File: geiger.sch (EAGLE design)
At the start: 4 parts, among them IC1 74LS14D, IC4 ICL7621SA

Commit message: Picking parts
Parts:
- removed D1: 1N821, diode:1N821
- removed IC4: ICL7621SA, maxim:ICL7621SA
- added C1, C10, C11, C12, C13, C14, C15, C16, C2, C3, C4, C5, C6, C7, C8, C9: (no value), rcl:C-EUC0603
- added D10, D11, D12, D13, D14, D15, D16, D17, D2, D3, D4, D5, D6, D7, D8, D9: 1N4148DO35-7, diode:1N4148DO35-7
- added IC2: LM4041A12DBZ, texas:LM4041A12DBZ
- added IC3: MAX4105EUK, maxim:MAX4105EUK
- added L1: (no value), rcl:L-US6000-XXX-RC
- added R1, R2, R3, R4, R5: (no value), resistor:R-EU_R0603
- added R6: (no value), rcl:R-TRIMM4G/J
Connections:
- new net F/B: IC3G$1.-IN, R4.1, R5.2
- new net N$10: C3.2, C5.1, D5.A
- new net N$11: R6.E
- new net N$12: C5.2, C7.1, D6.C, D7.A
- new net N$13: C6.2, C8.1, D7.C, D8.A
- new net N$14: C7.2, C9.1, D8.C, D9.A
- new net N$15: C10.1, C8.2, D10.A, D9.C
- new net N$16: C11.1, C9.2, D10.C, D11.A
- new net N$17: C11.2, C13.1, D12.C, D13.A
- new net N$18: C13.2, C15.1, D14.C, D15.A
- new net N$19: C15.2, D16.C, D17.A
- new net N$2: D2.A, R3.1
- new net N$20: C16.2, D17.C
- new net N$21: C14.2, C16.1, D15.C, D16.A
- new net N$22: C12.2, C14.1, D13.C, D14.A
- new net N$23: C10.2, C12.1, D11.C, D12.A
- new net N$24: C3.1, D3.A, L1.2
- new net N$7: C2.2, C4.1, D3.C, D4.A, R4.2
- new net N$8: C4.2, C6.1, D5.C, D6.A
- net GND: now also C1.2, C2.1, IC2.A, R6.S; no longer D1.A, IC4A.V-
- net N$1: now also IC2.C, IC3G$1.+IN, R1.1; no longer D1.C, IC4A.+IN
- net N$3: now also IC3G$1.OUT, R2.2; no longer IC4A.OUT
- net N$4: now also C1.1, R2.1, R3.2
- net N$5: now also D2.C
- net VCC: now also L1.1, R1.2; no longer IC4A.V+
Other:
- moved on the sheet: Q1

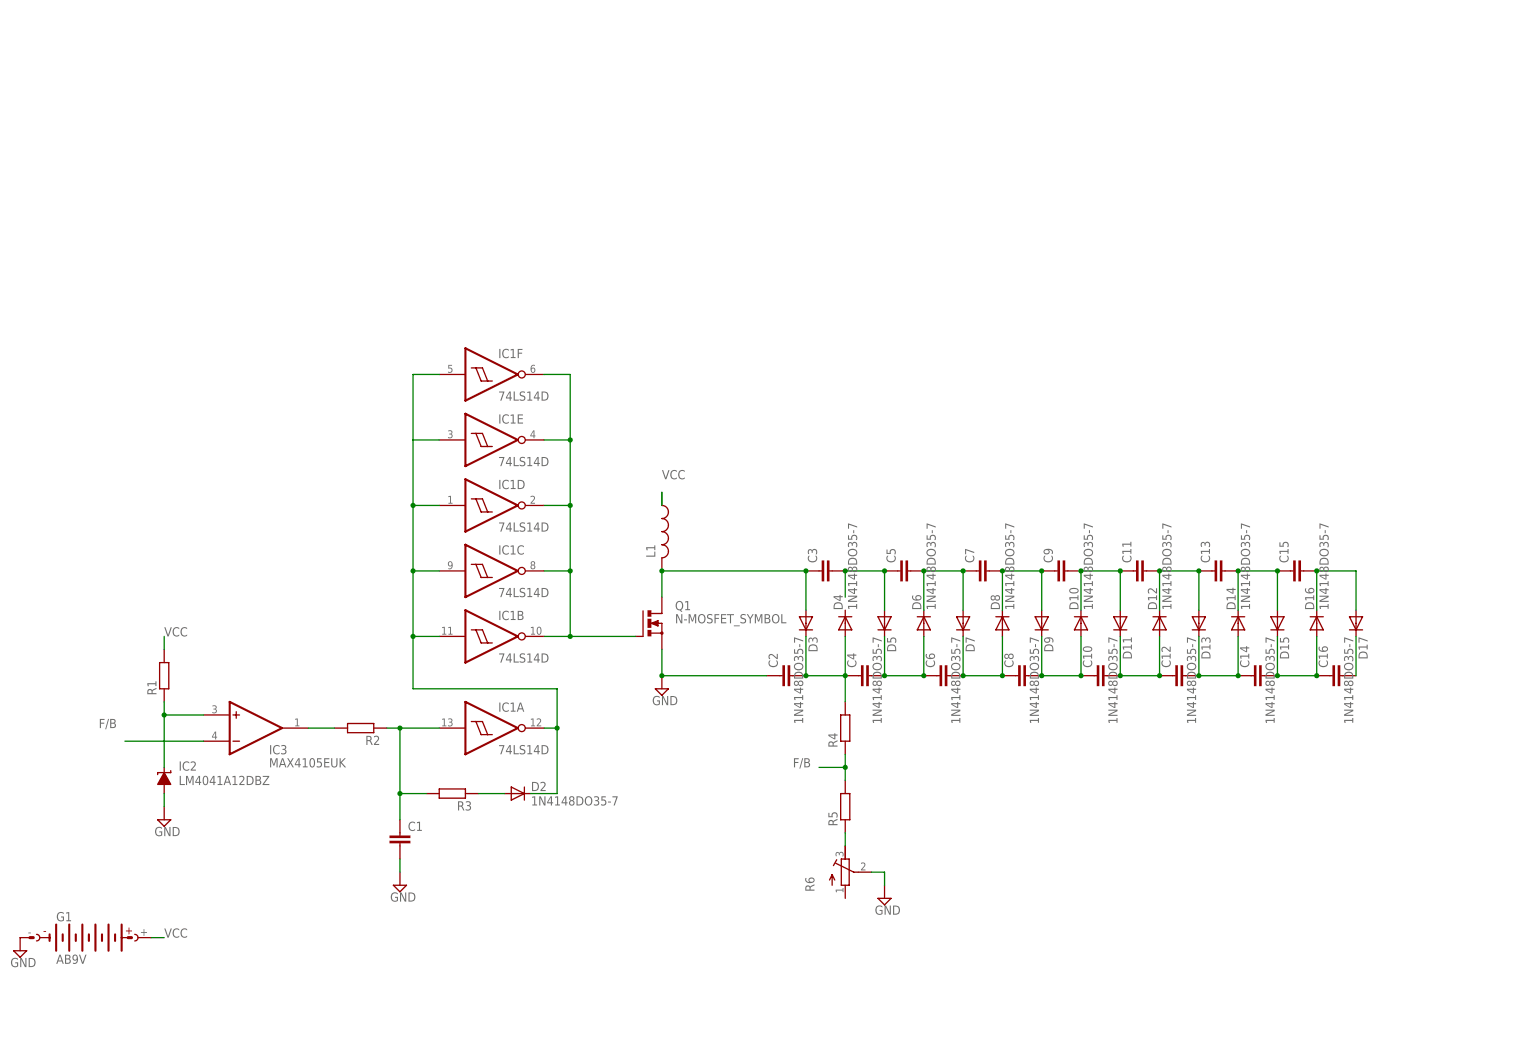
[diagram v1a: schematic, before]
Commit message: Completeing power supply on board
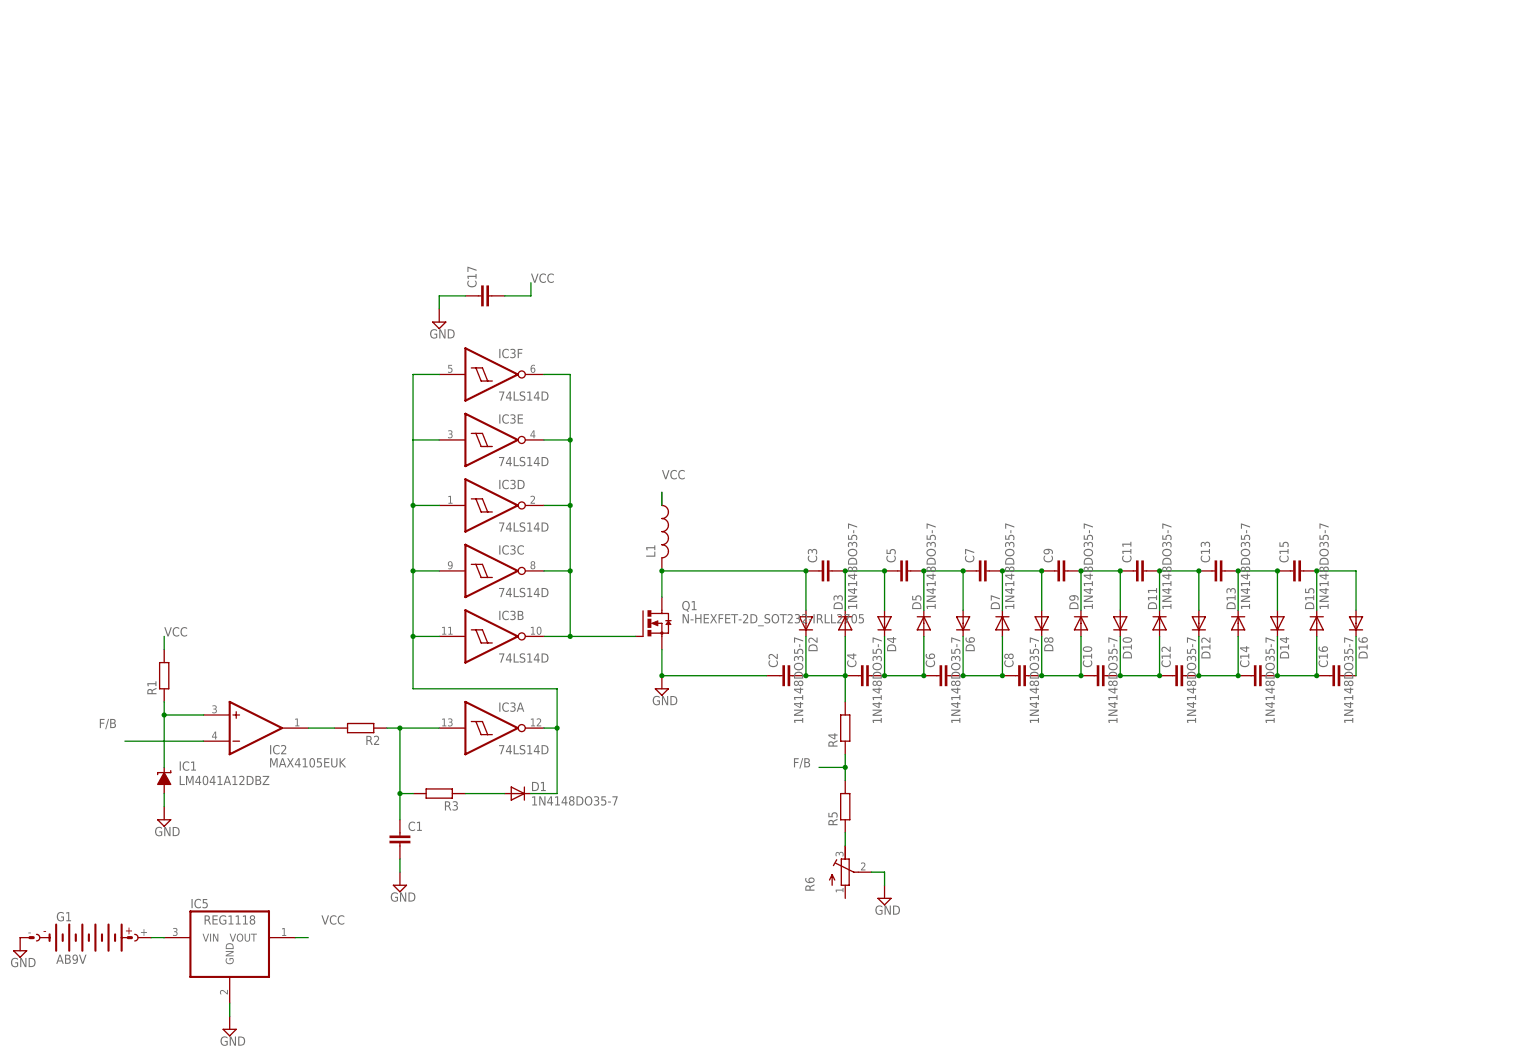
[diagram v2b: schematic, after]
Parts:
- removed D17: 1N4148DO35-7, diode:1N4148DO35-7
- added C17: (no value), rcl:C-EUC0603
- added D1: 1N4148DO35-7, diode:1N4148DO35-7
- added IC5: REG1118, burr-brown:REG1118
- added Q1: N-HEXFET-2D_SOT232-IRLL2705, transistor-power:N-HEXFET-2D_SOT232-IRLL2705
- IC1: value 74LS14D -> LM4041A12DBZ; device 74xx-us:74LS14D -> texas:LM4041A12DBZ
- IC2: value LM4041A12DBZ -> MAX4105EUK; device texas:LM4041A12DBZ -> maxim:MAX4105EUK
- IC3: value MAX4105EUK -> 74LS14D; device maxim:MAX4105EUK -> 74xx-us:74LS14D
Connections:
- new net N$9: G1.+, IC5.VIN
- net F/B: now also IC2G$1.-IN; no longer IC3G$1.-IN
- net GND: now also C17.1, IC1.A, IC5.GND, Q1.S; no longer IC2.A
- net N$1: now also IC1.C, IC2G$1.+IN; no longer IC2.C, IC3G$1.+IN
- net N$10: now also D3.C, D4.A; no longer D5.A
- net N$11: now also R5.1
- net N$12: now also D5.C, D6.A; no longer D6.C, D7.A
- net N$13: now also D6.C, D7.A; no longer D7.C, D8.A
- net N$14: now also D7.C, D8.A; no longer D8.C, D9.A
- net N$15: now also D8.C, D9.A; no longer D10.A, D9.C
- net N$16: now also D10.A, D9.C; no longer D10.C, D11.A
- net N$17: now also D11.C, D12.A; no longer D12.C, D13.A
- net N$18: now also D13.C, D14.A; no longer D14.C, D15.A
- net N$19: now also D15.C, D16.A; no longer D16.C, D17.A
- net N$2: now also D1.A; no longer D2.A
- net N$20: now also D16.C; no longer D17.C
- net N$21: now also D14.C, D15.A; no longer D15.C, D16.A
- net N$22: now also D12.C, D13.A; no longer D13.C, D14.A
- net N$23: now also D10.C, D11.A; no longer D11.C, D12.A
- net N$24: now also D2.A, Q1.D; no longer D3.A
- net N$3: now also IC2G$1.OUT; no longer IC3G$1.OUT
- net N$4: now also IC3A.I; no longer IC1A.I
- net N$5: now also D1.C, IC3A.O, IC3B.I, IC3C.I, IC3D.I, IC3E.I, IC3F.I; no longer D2.C, IC1A.O, IC1B.I, IC1C.I, IC1D.I, IC1E.I, IC1F.I
- net N$6: now also IC3B.O, IC3C.O, IC3D.O, IC3E.O, IC3F.O, Q1.G; no longer IC1B.O, IC1C.O, IC1D.O, IC1E.O, IC1F.O
- net N$7: now also D2.C, D3.A; no longer D3.C, D4.A
- net N$8: now also D4.C, D5.A; no longer D5.C, D6.A
- net VCC: now also C17.2, IC5.VOUT; no longer G1.+
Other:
- moved on the sheet: D10, D11, D12, D13, D14, D15, D16, D2, D3, D4, D5, D6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

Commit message: Up to date with built Rev1
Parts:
- removed G1: AB9V, battery:AB9V
- removed IC5: REG1118, burr-brown:REG1118
- added C18: 1000uF, rcl:CPOL-USTT5D10
- added C19: 1uf, rcl:C-EUC0603
- added U$1, U$2, U$3, U$5: BINDING-POST, geiger:BINDING-POST
- C1: value (none) -> 100pF
- C10, C11, C12, C13, C14, C15, C16, C2, C3, C4, C5, C6, C7, C8, C9: value (none) -> 0.1uF
- C17: value (none) -> 1uf
- IC1: value LM4041A12DBZ -> 2.5V
- L1: value (none) -> 4.7uH
- R1: value (none) -> 750k
- R2: value (none) -> 100k
- R3: value (none) -> 10k
- R4: value (none) -> 68M
- R5: value (none) -> 2M
- R6: value (none) -> 500k
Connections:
- net N$19 renamed +HV
- removed net N$20: C16.2, D16.C
- removed net N$9: G1.+, IC5.VIN
- new net HV: C16.2, D16.C, U$5.1
- net GND: now also C18.-, C19.1, U$1.1, U$3.1; no longer G1.-, IC5.GND
- net VCC: now also C18.+, C19.2, U$2.1; no longer IC5.VOUT
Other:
- note added: "1"
- note added: "1/1"
- note added: "2016/09/11"
- note added: "CEPS GM-COUNTER"
- note added: "High Voltage Step-Up Converter"
- moved on the sheet: C1, C17, D1, IC1, IC2, IC3A, IC3B, IC3C, IC3D, IC3E, IC3F, L1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
